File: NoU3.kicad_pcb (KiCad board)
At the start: 4 copper layers, 46 x 56 mm, 135 parts, among them J1 JST SR/SZ, J10 JST SR/SZ, J11 Screw_Terminal_01x02, J12 Screw_Terminal_01x02, J13 JST SR/SZ, J14 RFANT3216120A5T, J15 Barrel_Jack, J16 JST SR/SZ, J17 JST SR/SZ, J2 Screw_Terminal_01x02, J3 Screw_Terminal_01x02, J4 JST SR/SZ, J5 Screw_Terminal_01x02, J6 Screw_Terminal_01x02, J7 JST SR/SZ, J8 Screw_Terminal_01x02, J9 Screw_Terminal_01x02, Q1 AO3401A, SW1 reset, SW2 boot, U1 HR8833, U13 74HC595, U14 74HC595, U15 SY8113BADC, U16 SY8113BADC, U17 USB_C_Receptacle, U18 ServoPorts_2x3, U19 ServoPorts_2x3, U2 ESP32-S3FN8, U23 BMI270, U25 MMC5983MA, U26 LSM6DSO, U3 Crystal_ESP32, U4 HR8833, U5 HR8833, U6 HR8833, U7 ServoPorts_2x3, U8 XKB5858-Z-75, U9 USBLC6-2P6

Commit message: initial V3.2 changes
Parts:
- removed C20, C39: 82uF, AlfredoFootprints:Cap_THT_82uF_5mm_2mm
- removed C41: 100nF, Capacitor_SMD:C_0402_1005Metric
- removed D4: LED_red, AlfredoFootprints:LED_3mm
- removed JP1, JP2: SolderJumper_2_Open, Jumper:SolderJumper-2_P1.3mm_Open_RoundedPad1.0x1.5mm
- removed R31: 1K, Resistor_SMD:R_0402_1005Metric
- removed TP16, TP17, TP5, TP8, TP9: GND, AlfredoFootprints:PogoPad1
- removed TP22: nSleep, AlfredoFootprints:PogoPad1
- removed TP6: qwiic_sda, AlfredoFootprints:PogoPad1
- removed TP7: qwiic_scl, AlfredoFootprints:PogoPad1
- removed U13, U14: 74HC595, Package_SO:TSSOP-16_4.4x5mm_P0.65mm
- removed U23: BMI270, Package_LGA:Bosch_LGA-14_3x2.5mm_P0.5mm
- added C16: ~, Capacitor_SMD:CP_Elec_6.3x7.7, F.Cu at (-10.4, -12.7)
- added U10: PCA9685BS, Package_DFN_QFN:QFN-28-1EP_6x6mm_P0.65mm_EP4.25x4.25mm, F.Cu at (-11.5, -5.00)
- added U11: Qwiic1, Connector_JST:JST_SH_BM04B-SRSS-TB_1x04-1MP_P1.00mm_Vertical, F.Cu at (-19.1, 26.7)
- R29: value 1K -> 3K
- TP4: value GND -> ECLK
- moved R23 58.7 mm to (-38.7, 4.60), turned to 0 degrees
- moved TP4 54.6 mm to (-43.2, 5.71)
- moved SW1 23.2 mm to (7.00, 27.3)
- moved SW2 13.2 mm to (-7.00, 27.3)
- moved R19 12.5 mm to (5.21, 38.7)
- moved C40 10.8 mm to (5.21, 36.5)
- moved C42 10.8 mm to (-4.89, 38.5)
- moved C43 10.8 mm to (-4.89, 36.5)
- moved R22 10.8 mm to (0.31, 38.5)
- moved R28 10.8 mm to (0.31, 36.5)
- moved U25 10.8 mm to (-2.29, 37.5)
- moved U26 10.8 mm to (2.71, 37.5)
- moved TP10 7.26 mm to (-6.99, 32.4)
- moved TP15 7.22 mm to (3.17, 32.4)
- moved J5 0.05 mm to (-19.0, -11.0)
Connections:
- J16 pad 6: GPIO_MISC2 -> unconnected-(J16-Pin_6-Pad6)
- R18 pad 1: LED_MISC1 -> LED_MISC
- R19 pad 1: Net-(U23-SDO) -> +3V3
- R19 pad 2: GND -> Net-(U26-CSB)
- R23 pad 1: SF_INT1 -> +3V3
- R23 pad 2: GND -> M_OE
- R25 pad 1: GPIO_MISC2 -> SF_INT1
- U2 pad 17: M_SRCLK -> M_OE
- U2 pad 18: M_RCLK -> unconnected-(U2-GPIO13-Pad18)
- U2 pad 19: M_SER -> unconnected-(U2-GPIO14-Pad19)
- U2 pad 36: GPIO_MISC1 -> GPIO_MISC
- U2 pad 37: GPIO_MISC2 -> unconnected-(U2-SPICLK_P-Pad37)
- U25 pad 15: GPIO_MISC2 -> SF_INT1
- U26 pad 12: Net-(JP2-B) -> Net-(U26-CSB)
- U26 pad 2: Net-(U26-SDx) -> GND
- U26 pad 3: Net-(U26-SCx) -> GND
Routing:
- net nSleep: track 69.7 -> 0.00 mm, vias 6 -> 0
- net GND: track 103.0 -> 64.2 mm, vias 67 -> 57
- net M_RCLK: track 31.8 -> 0.00 mm, vias 3 -> 0
- net M_SRCLK: track 31.3 -> 0.00 mm, vias 3 -> 0
- net SF_SCL: track 69.5 -> 38.9 mm, vias 5 -> 2
- net SF_SDA: track 69.9 -> 39.8 mm, vias 5 -> 2
- net +3V3: track 68.2 -> 40.5 mm, vias 27 -> 16
- net SF_INT1: track 62.9 -> 35.9 mm, vias 3 -> 1
- net M_SER: track 25.0 -> 0.00 mm, vias 2 -> 0
- net SF_INT2: track 64.0 -> 45.9 mm, vias 3 -> 2
- net GPIO_MISC2: track 69.9 -> 52.0 mm, vias 4 -> 3
- net /MotorDriver-2/BIN1: track 24.3 -> 11.6 mm, vias 2 -> 1
- net LED_MISC2: track 19.6 -> 8.71 mm
- net M_OE: track 0.00 -> 9.99 mm, vias 0 -> 1
- net VCC: track 89.5 -> 80.0 mm
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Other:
- board text added: "3K/1K => 0.25*3.3V"
- board text added: "Alfredo NoU V3.2"
- board text added: "Qwiic"
- board text removed: "1K/1K => 0.5*3.3V"
- board text removed: "Alfredo NoU V3.1"
- board text removed: "NSLP"
- board text removed: "SCL"
- board text removed: "SDA"

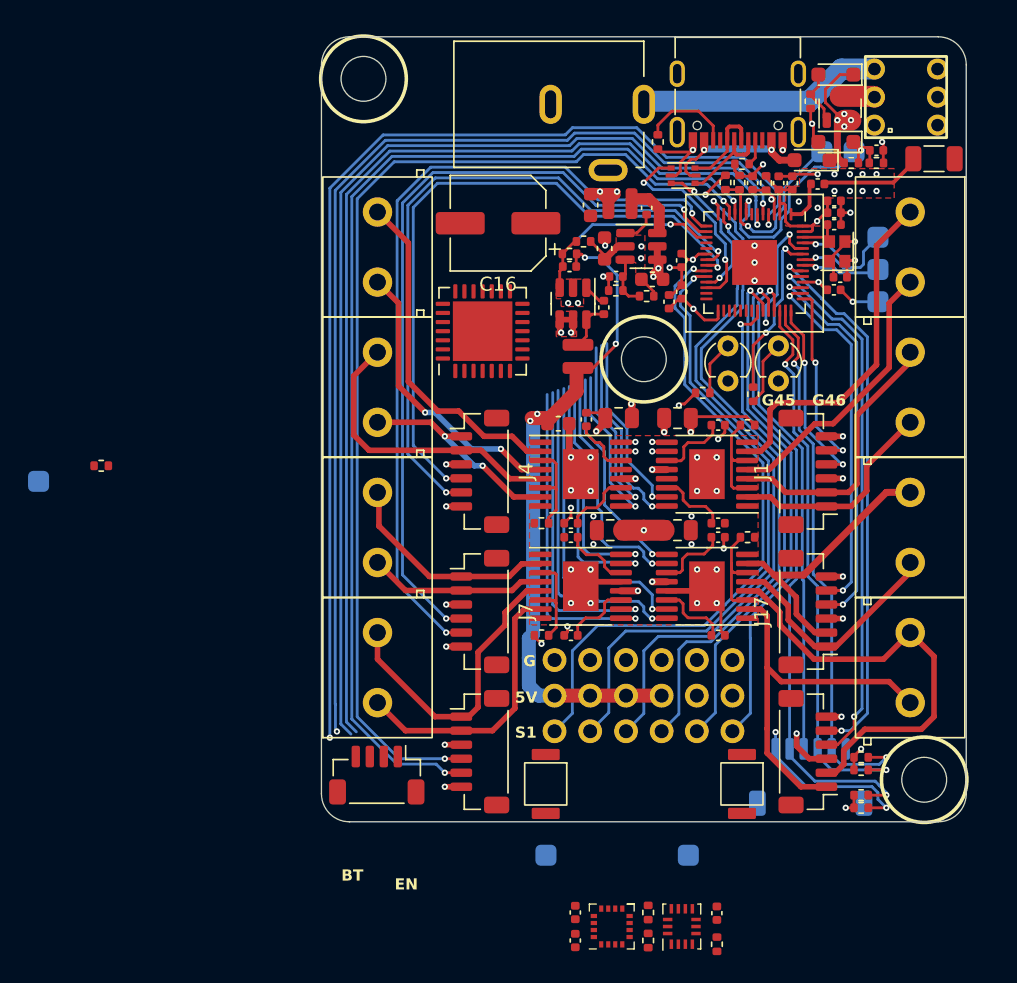
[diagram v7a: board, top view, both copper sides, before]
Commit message: order candidate, layout complete
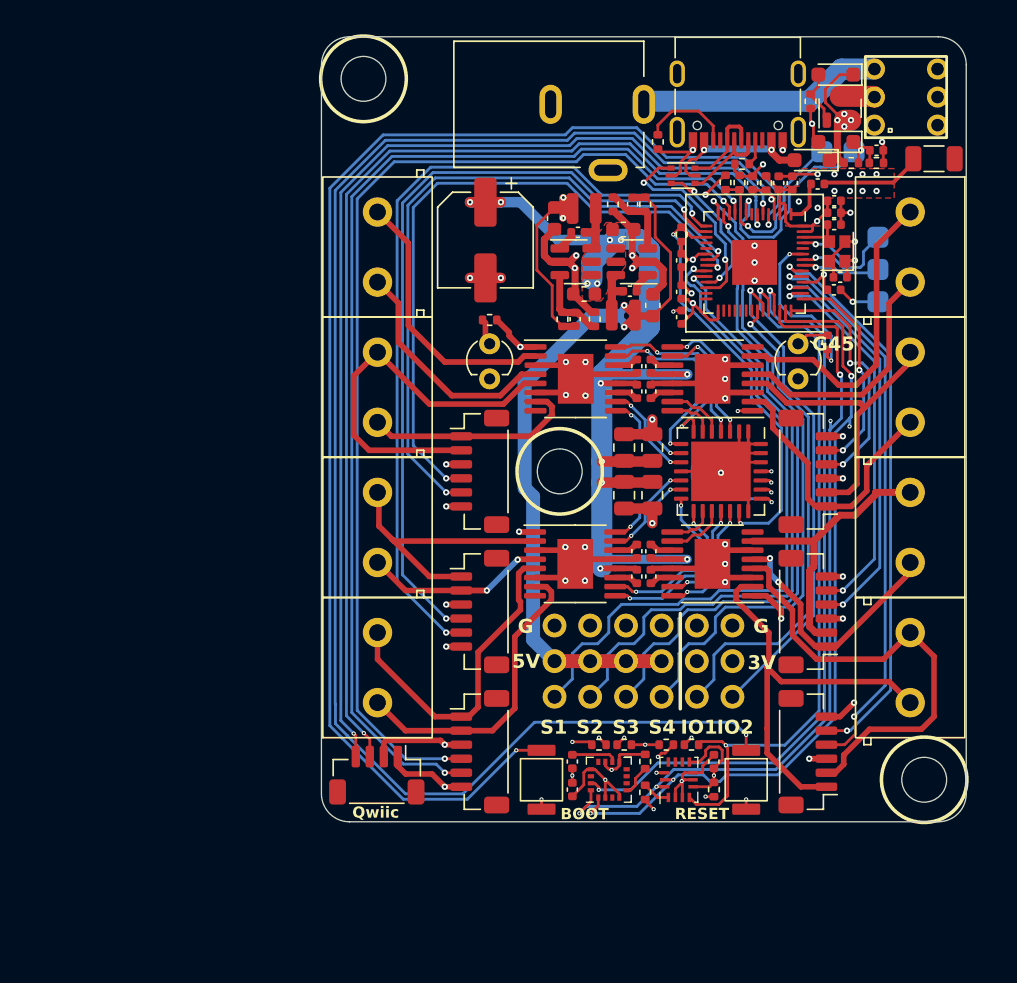
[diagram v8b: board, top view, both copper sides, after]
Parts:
- removed J16: JST SR/SZ, Connector_JST:JST_SH_SM06B-SRSS-TB_1x06-1MP_P1.00mm_Horizontal
- removed R1, R3, R6, R8: 0.1R, Resistor_SMD:R_0402_1005Metric
- removed TP10, TP15: GND, AlfredoFootprints:PogoPad1
- moved TP4 47.3 mm to (4.10, 5.10)
- moved R23 44.6 mm to (2.70, -11.9), turned to 90 degrees
- moved U10 19.7 mm to (5.50, 5.00), turned to -90 degrees
- moved R25 19.2 mm to (-3.20, 24.5), turned to 0 degrees
- moved D5 17.0 mm to (-11.0, -1.60)
- moved R21 17.0 mm to (-1.40, 24.5), turned to 180 degrees
- moved R17 16.1 mm to (-11.0, -5.80), turned to 180 degrees
- moved R20 13.9 mm to (1.60, 24.5)
- moved R24 12.6 mm to (3.40, 24.5)
- moved R19 11.0 mm to (5.00, 27.7)
- moved C40 10.8 mm to (5.00, 25.7)
- moved C36 10.8 mm to (0.64, -6.85), turned to 90 degrees
- moved C42 10.8 mm to (-5.10, 27.7)
- moved C43 10.8 mm to (-5.10, 25.7)
- moved R28 10.8 mm to (0.10, 25.7)
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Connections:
- U1 pad 1: nSleep -> +3V3
- U1 pad 3: Net-(U1-AISEN) -> GND
- U1 pad 6: Net-(U1-AISEN) -> GND
- U10 pad 10: /MotorDriver-4/BIN1 -> /MotorDriver-2/BIN1
- U10 pad 12: /MotorDriver-2/BIN1 -> /MotorDriver-3/AIN1
- U10 pad 13: /MotorDriver-2/BIN2 -> /MotorDriver-3/AIN2
- U10 pad 14: /MotorDriver-1/AIN1 -> /MotorDriver-3/BIN2
- U10 pad 15: /MotorDriver-1/AIN2 -> /MotorDriver-3/BIN1
- U10 pad 16: /MotorDriver-1/BIN1 -> /MotorDriver-4/BIN1
- U10 pad 17: /MotorDriver-1/BIN2 -> /MotorDriver-4/BIN2
- U10 pad 18: /MotorDriver-2/AIN1 -> /MotorDriver-4/AIN2
- U10 pad 19: /MotorDriver-2/AIN2 -> /MotorDriver-4/AIN1
- U10 pad 3: /MotorDriver-3/BIN1 -> /MotorDriver-1/BIN1
- U10 pad 4: /MotorDriver-3/BIN2 -> /MotorDriver-1/BIN2
- U10 pad 5: /MotorDriver-4/AIN1 -> /MotorDriver-1/AIN2
- U10 pad 6: /MotorDriver-4/AIN2 -> /MotorDriver-1/AIN1
- U10 pad 7: /MotorDriver-3/AIN2 -> /MotorDriver-2/AIN1
- U10 pad 8: /MotorDriver-3/AIN1 -> /MotorDriver-2/AIN2
- U10 pad 9: /MotorDriver-4/BIN2 -> /MotorDriver-2/BIN2
- U2 pad 27: nSleep -> unconnected-(U2-GPIO21-Pad27)
- U2 pad 36: GPIO_MISC -> GPIO_MISC1
- U2 pad 37: unconnected-(U2-SPICLK_P-Pad37) -> GPIO_MISC2
- U2 pad 51: LED_MISC1 -> LED_MISC
- U2 pad 52: LED_MISC2 -> unconnected-(U2-GPIO46-Pad52)
- U26 pad 9: Net-(U26-INT2) -> unconnected-(U26-INT2-Pad9)
- U4 pad 1: nSleep -> +3V3
- U4 pad 3: Net-(U4-AISEN) -> GND
- U4 pad 6: Net-(U4-AISEN) -> GND
- U5 pad 1: nSleep -> +3V3
- U5 pad 3: Net-(U5-AISEN) -> GND
- U5 pad 6: Net-(U5-AISEN) -> GND
- U6 pad 1: nSleep -> +3V3
- U6 pad 3: Net-(U6-AISEN) -> GND
- U6 pad 6: Net-(U6-AISEN) -> GND
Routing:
- net GND: track 64.2 -> 147.7 mm, vias 57 -> 61
- net +3V3: track 40.5 -> 78.8 mm, vias 16 -> 21
- net Net-(U2-CHIP_PU): track 76.6 -> 110.9 mm
- net SF_SCL: track 38.9 -> 69.0 mm, vias 2 -> 6
- net SF_SDA: track 39.8 -> 69.3 mm, vias 2 -> 6
- net VCC: track 80.0 -> 104.2 mm, vias 20 -> 16
- net SF_INT1: track 35.9 -> 59.4 mm, vias 1 -> 3
- net M_OE: track 9.99 -> 30.1 mm, vias 1 -> 2
- net Net-(U2-GPIO0): track 78.2 -> 96.1 mm
- net GPIO_MISC2: track 52.0 -> 35.1 mm, vias 3 -> 1
- net /MotorDriver-4/AIN2: track 22.4 -> 7.99 mm, vias 1 -> 2
- net /MotorDriver-4/AIN1: track 23.2 -> 8.86 mm, vias 1 -> 2
- net /MotorDriver-4/BIN2: track 17.5 -> 4.24 mm, vias 1 -> 0
- net LED_MISC1: track 12.2 -> 0.00 mm, vias 2 -> 0
- net /MotorDriver-4/BIN1: track 15.5 -> 3.28 mm, vias 1 -> 0
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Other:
- board text added: "3V"
- board text added: "BOOT"
- board text added: "IO1"
- board text added: "IO2"
- board text added: "RESET"
- board text added: "S2"
- board text added: "S3"
- board text added: "S4"
- board text removed: "BT"
- board text removed: "EN"
- board text removed: "G46"
